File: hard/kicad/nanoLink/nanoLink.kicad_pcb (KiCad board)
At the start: 2 copper layers, 39.4 x 21.6 mm, 8 parts, among them J1 IOx, J2 nanoLink, U1 74HC139, U2 74HC174

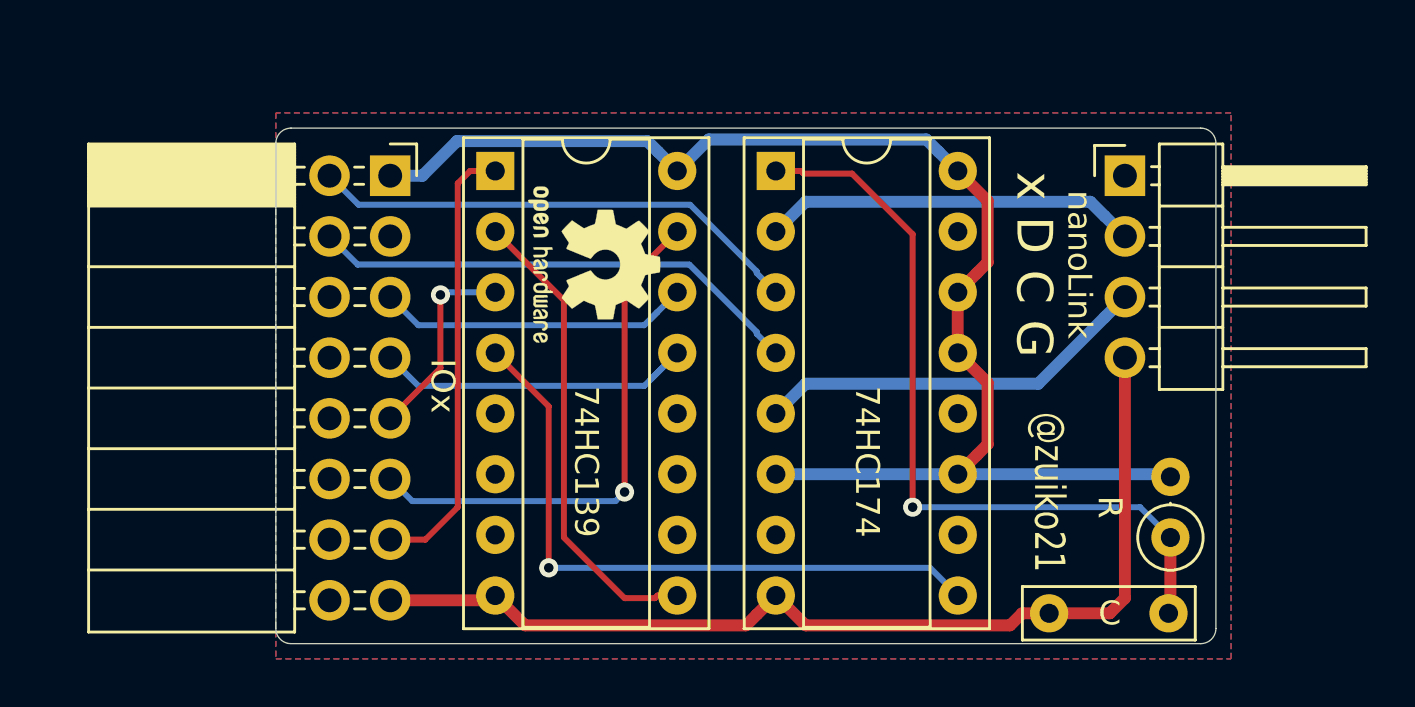
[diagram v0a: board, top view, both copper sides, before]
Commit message: rework nanoLink interface PCB
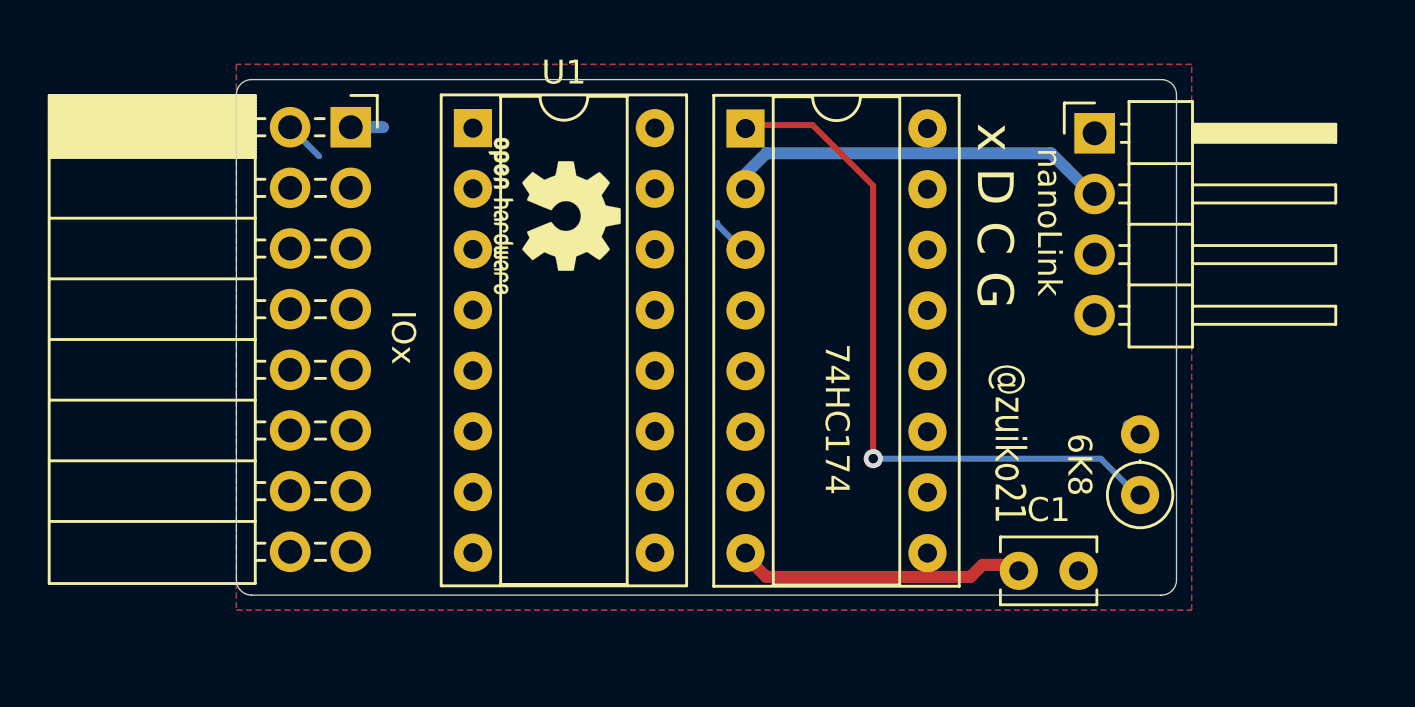
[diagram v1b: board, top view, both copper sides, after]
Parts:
- C1: value C -> 68pF; footprint Capacitor_THT:C_Rect_L7.0mm_W2.0mm_P5.00mm -> Capacitor_THT:C_Disc_D3.8mm_W2.6mm_P2.50mm
- R1: value R -> 6K8
- U1: value 74HC139 -> 74HC138
- moved J1 2.62 mm to (15.2, 12.7)
- moved LOGO1 2.62 mm to (23.7, 16.4)
- moved LOGO2 2.62 mm to (25.7, 21.5)
- moved C1 2.18 mm to (43.2, 31.2)
- moved J2 2.18 mm to (46.4, 12.9)
- moved R1 2.18 mm to (48.3, 28.1)
- moved U2 2.18 mm to (31.7, 12.7)
- moved U1 2.02 mm to (20.3, 12.7)
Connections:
- J1 pad 3: (no net) -> /BA0
- U1 pad 1: /~IOX -> /BA1
- U1 pad 12: (no net) -> /~SEND
- U1 pad 13: /BA2 -> (no net)
- U1 pad 14: /BA1 -> (no net)
- U1 pad 15: /~BWR -> (no net)
- U1 pad 2: /~SEL -> /BA2
- U1 pad 4: /~SEND -> /~BWR
- U1 pad 5: (no net) -> /~IOX
- U1 pad 6: (no net) -> /BA0
- U1 pad 9: /~SEL -> (no net)
- U2 pad 14: +5V -> /PD1
- U2 pad 15: (no net) -> /SERCLK
- U2 pad 4: /PD1 -> +5V
- U2 pad 5: /SERCLK -> (no net)
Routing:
- net +5V: track 57.3 -> 1.51 mm
- net GND: track 42.9 -> 12.2 mm
- net /~SEND: track 27.5 -> 0.00 mm, vias 1 -> 0
- net /~BWR: track 22.2 -> 0.00 mm, vias 1 -> 0
- net /PD1: track 20.8 -> 0.00 mm
- net /~SEL: track 19.8 -> 0.00 mm
- net /~IOX: track 18.7 -> 0.00 mm
- net /PD0: track 20.8 -> 2.92 mm
- net /SERCLK: track 16.6 -> 0.00 mm
- net /BA2: track 14.7 -> 0.00 mm
- net /BA1: track 13.5 -> 0.00 mm
- net /BA3: track 8.38 -> 0.00 mm, vias 1 -> 0
- net /~RST: track 32.8 -> 29.6 mm
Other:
- board text added: "nanoLink interface v1 2023·05"
- board text removed: "nanoLink interface v1 2023·01"

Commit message: finish nanoLink board
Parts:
- moved R1 2.41 mm to (48.3, 30.5)
- moved C1 0.99 mm to (42.5, 30.5)
- moved J2 0.67 mm to (45.7, 12.7)
- moved J1 0.05 mm to (15.2, 12.7)
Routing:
- net +5V: track 1.51 -> 65.5 mm
- net GND: track 12.2 -> 43.0 mm
- net /PD1: track 0.00 -> 29.9 mm, vias 0 -> 1
- net /PD0: track 2.92 -> 25.9 mm
- net /~SEND: track 0.00 -> 16.8 mm
- net /BA0: track 0.00 -> 13.8 mm
- net /SERCLK: track 0.00 -> 7.42 mm
- net /~IOX: track 0.00 -> 7.18 mm
- net /BA1: track 0.00 -> 7.18 mm
- net /BA2: track 0.00 -> 7.18 mm
- net /~BWR: track 0.00 -> 7.18 mm
- net /BA3: track 0.00 -> 7.18 mm
- net /~RST: track 29.6 -> 32.7 mm, vias 1 -> 2
- net /SERDAT: track 15.7 -> 15.0 mm
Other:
- board size 39.4 x 21.6 mm -> 39.4 x 21.8 mm

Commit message: nanoLink board ready for ordering
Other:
- board text added: "JLCJLCJLCJLC"
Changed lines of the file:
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@@
   (general
     (thickness 1.6)
-    (drawings 18)
+    (drawings 19)
     (tracks 83)
     (zones 0)
@@
     )
   )
+  (gr_text JLCJLCJLCJLC (at 33.655 16.637 270) (layer F.SilkS)
+    (effects (font (size 1 1) (thickness 0.15)))
+  )
   (gr_text "nanoLink interface\nv1 2023·05" (at 34.925 24.638 270) (layer B.SilkS)

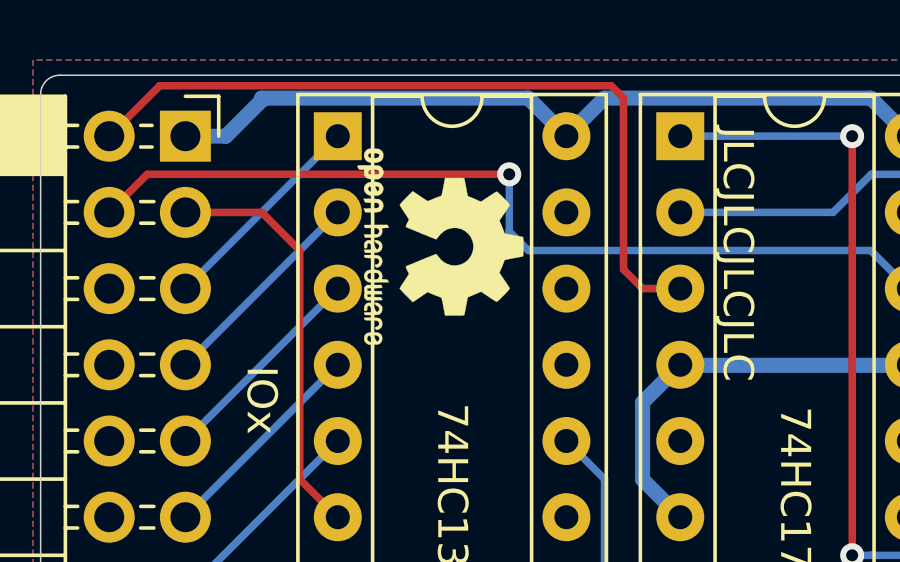
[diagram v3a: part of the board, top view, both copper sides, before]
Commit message: revised logos on nanoLink board
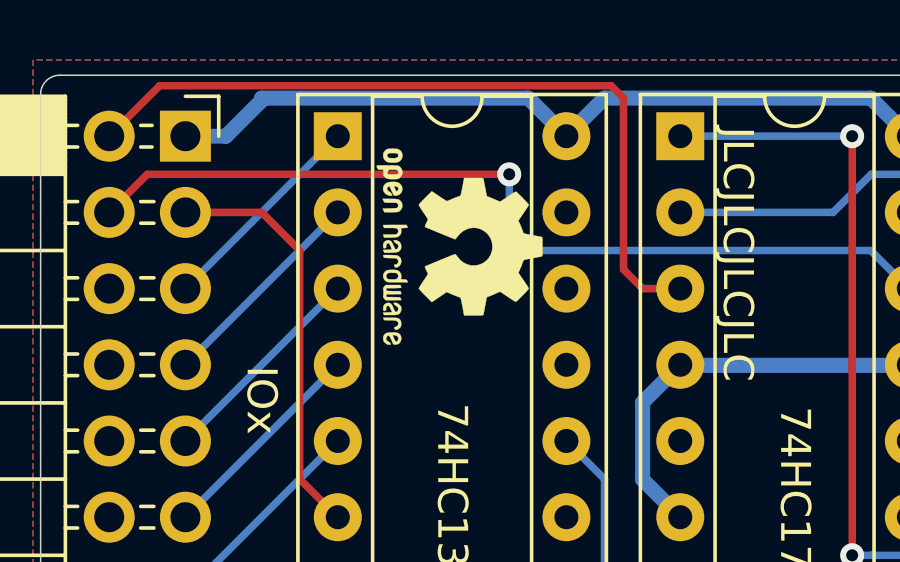
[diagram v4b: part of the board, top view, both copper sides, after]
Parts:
- LOGO2: footprint durango:jaqueria -> durango:j300
- moved LOGO2 19.6 mm to (45.1, 24.1)
- moved LOGO1 0.64 mm to (24.4, 16.4)
